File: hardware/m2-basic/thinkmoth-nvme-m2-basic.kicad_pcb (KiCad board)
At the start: 4 copper layers, 31 x 68.4 mm, 28 parts, among them J2 ExpressCard, J3 MDT180M03001

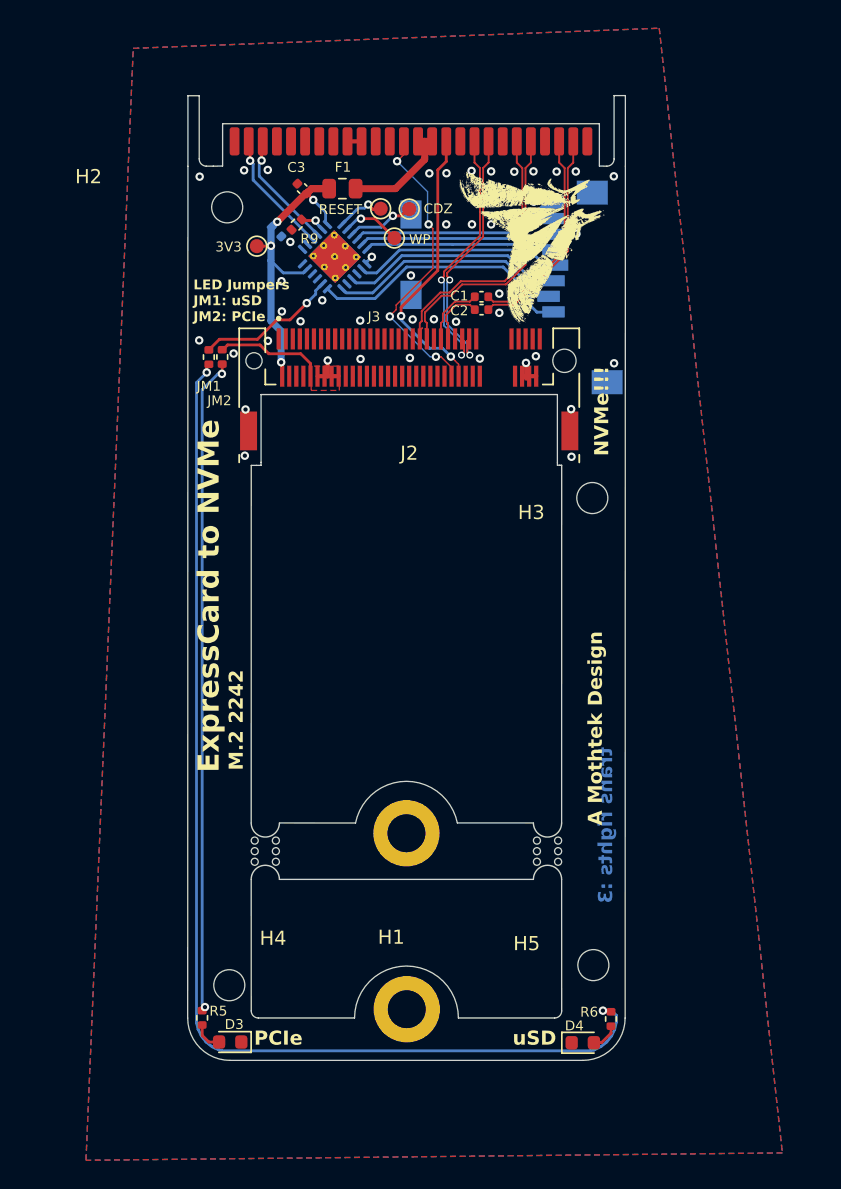
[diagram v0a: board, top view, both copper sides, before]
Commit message: m.2-basic: updated layout, moved mounting holes
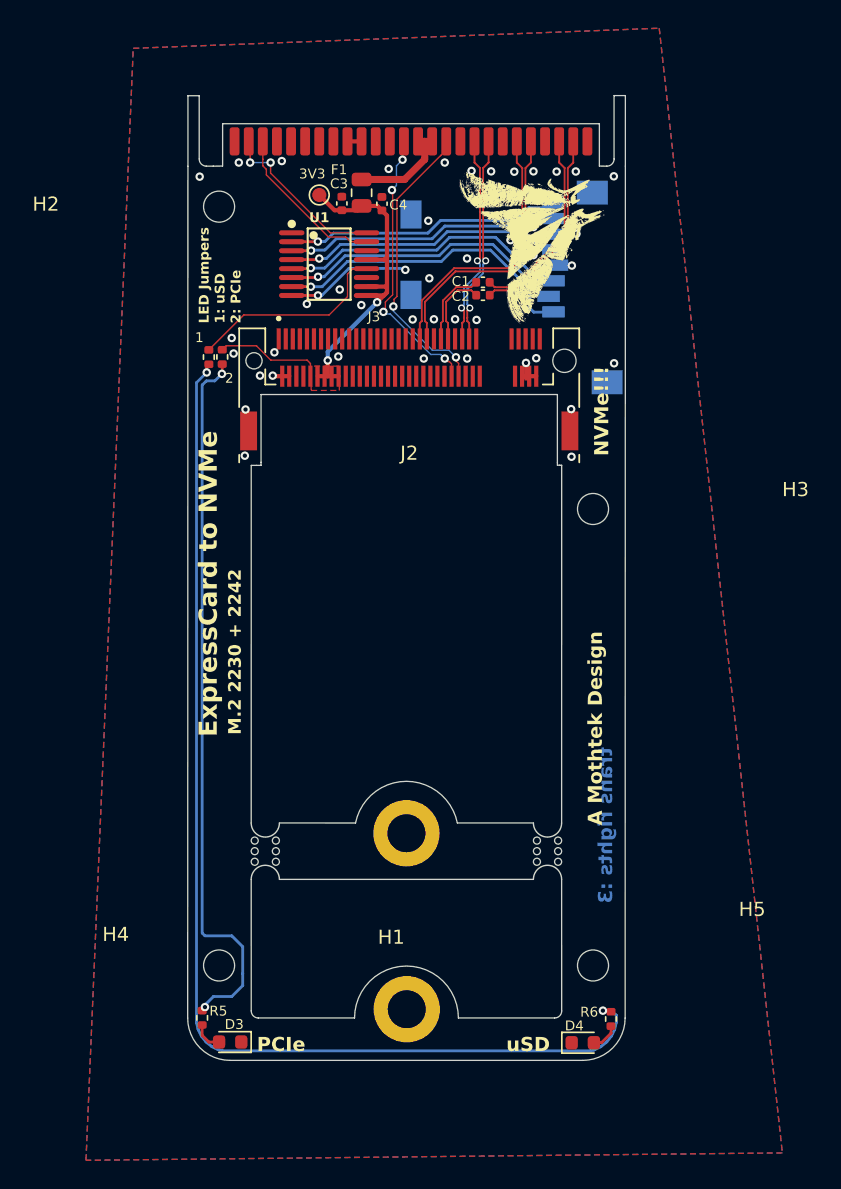
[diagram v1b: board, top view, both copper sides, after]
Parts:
- removed CDZ: SD_CDZ, TestPoint:TestPoint_Pad_D1.0mm
- removed R9: 680r, Resistor_SMD:R_0402_1005Metric
- removed RESET: SD_RESET, TestPoint:TestPoint_Pad_D1.0mm
- removed U2: ~, Package_DFN_QFN:QFN-24-1EP_4x4mm_P0.5mm_EP2.7x2.6mm_ThermalVias
- removed WP: SD_WP, TestPoint:TestPoint_Pad_D1.0mm
- added U1: GL823K-HCY04, GL823K-HCY04:SSOP-16_L4.9-W3.9-P0.64-LS6.0-BL, F.Cu at (70.2, 61.2)
- C4: moved to F.Cu
- moved C4 7.73 mm to (73.9, 56.9), turned to -90 degrees
- moved 3V3 5.72 mm to (69.5, 56.3)
- moved C3 3.00 mm to (71.1, 56.9), turned to -90 degrees
- moved H4 1.58 mm to (62.4, 110.9)
- moved F1 1.39 mm to (72.5, 56.1), turned to 90 degrees
- moved C1 1.03 mm to (81.1, 62.5)
- moved C2 1.03 mm to (81.1, 63.4)
- moved H3 0.78 mm to (88.9, 78.6)
- moved H2 0.58 mm to (62.4, 57.1)
- renumbered JM1 to 1, JM2 to 2, SD1 to Card1
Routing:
- net SD_3V3: track 15.1 -> 21.9 mm, vias 0 -> 3
- net 3V3: track 37.1 -> 30.7 mm, vias 7 -> 4
- net SD_CLK: track 13.5 -> 19.9 mm, vias 0 -> 1
- net SD_DAT0: track 14.3 -> 19.6 mm, vias 0 -> 1
- net SD_CDZ: track 4.95 -> 0.00 mm, vias 1 -> 0
- net SD_DAT1: track 14.8 -> 19.7 mm, vias 0 -> 1
- net SD_CMD: track 15.9 -> 20.7 mm, vias 0 -> 1
- net SD_LED: track 10.1 -> 14.5 mm, vias 1 -> 0
- net Net-(JM2-Pad1): track 46.7 -> 51.0 mm
- net SD_WP: track 4.25 -> 0.00 mm, vias 1 -> 0
- net SD_DAT3: track 16.7 -> 20.7 mm, vias 0 -> 1
- net SD_RESET: track 3.49 -> 0.00 mm, vias 1 -> 0
- net USB_N: track 8.82 -> 12.3 mm, vias 1 -> 2
- net PCIe_CLK_N: track 18.5 -> 15.0 mm
- net PCIe_CLK_P: track 18.5 -> 15.0 mm
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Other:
- board text added: "LED Jumpers 1: uSD 2: PCIe"
- board text added: "M.2 2230 + 2242"
- board text removed: "LED Jumpers JM1: uSD JM2: PCIe"
- board text removed: "M.2 2242"
